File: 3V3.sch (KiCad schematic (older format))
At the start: 42 parts, among them U10 LM21215, U11 LM21215, U14 INA214, U15 INA214

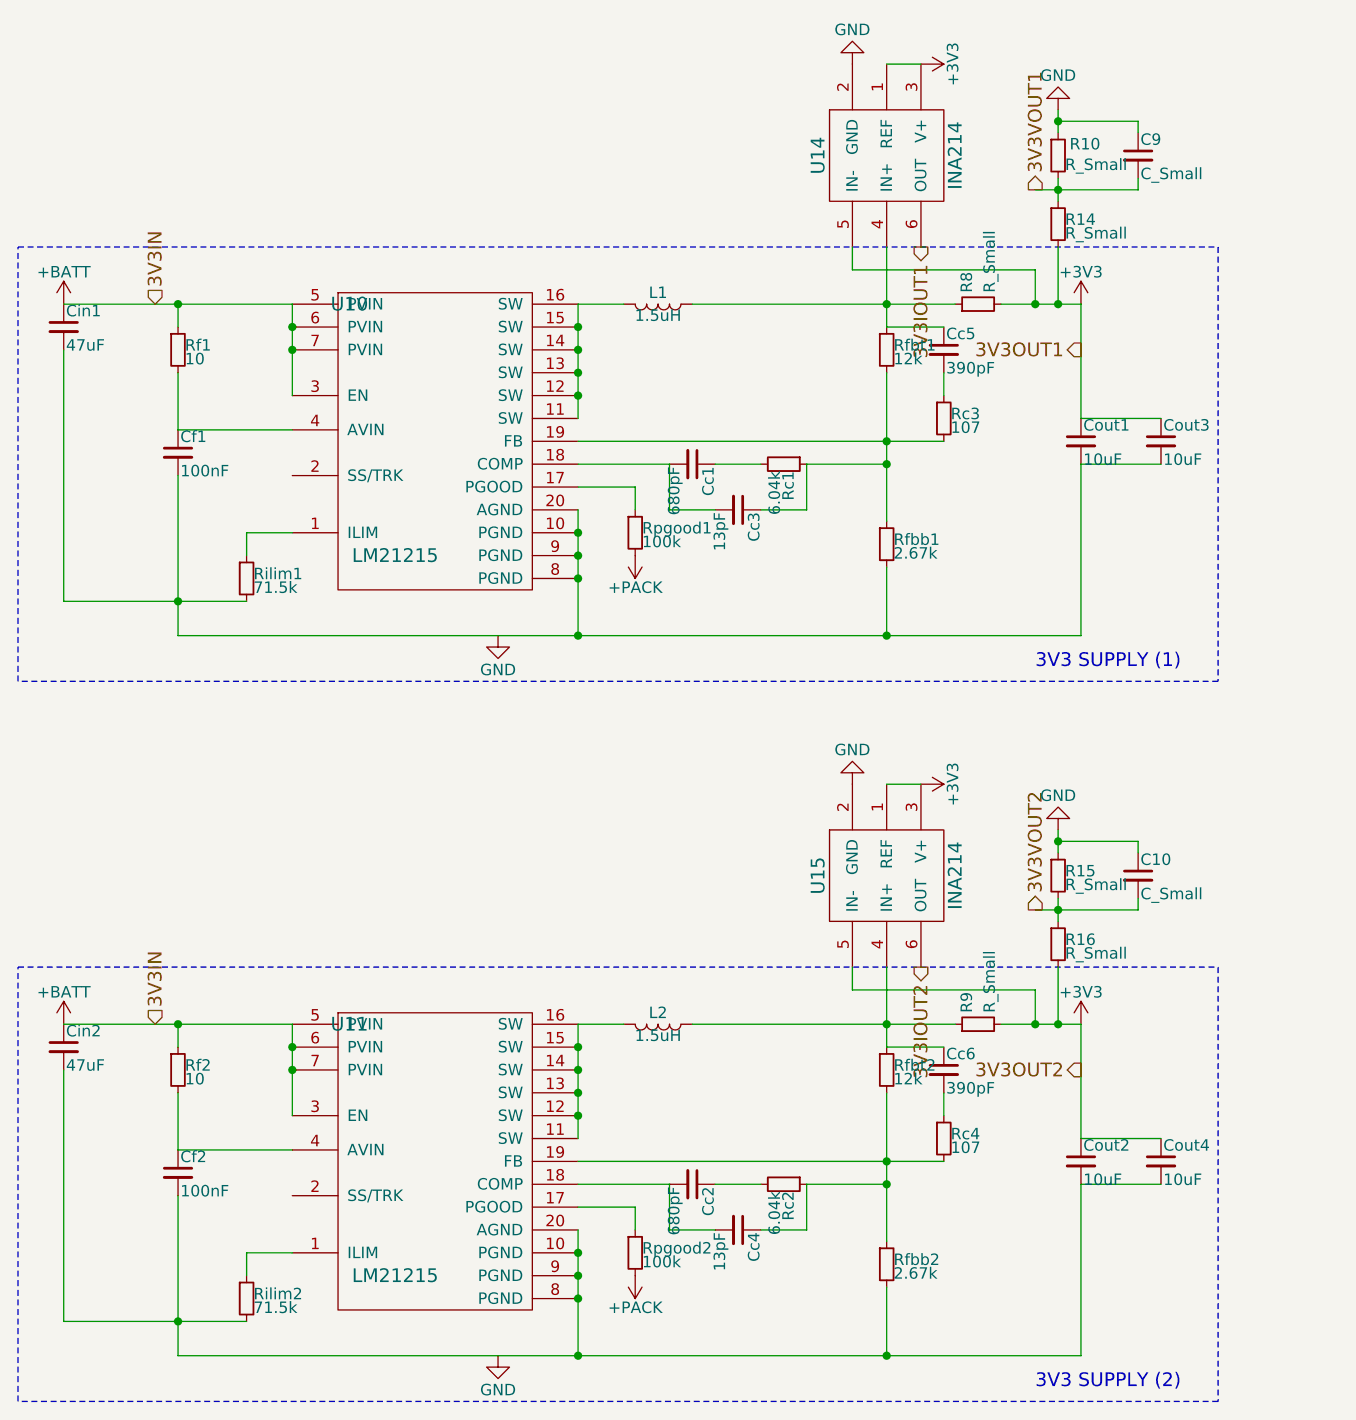
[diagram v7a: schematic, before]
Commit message: PCB layout as of 2018-02-12
All that’s left to do is add deployment switches
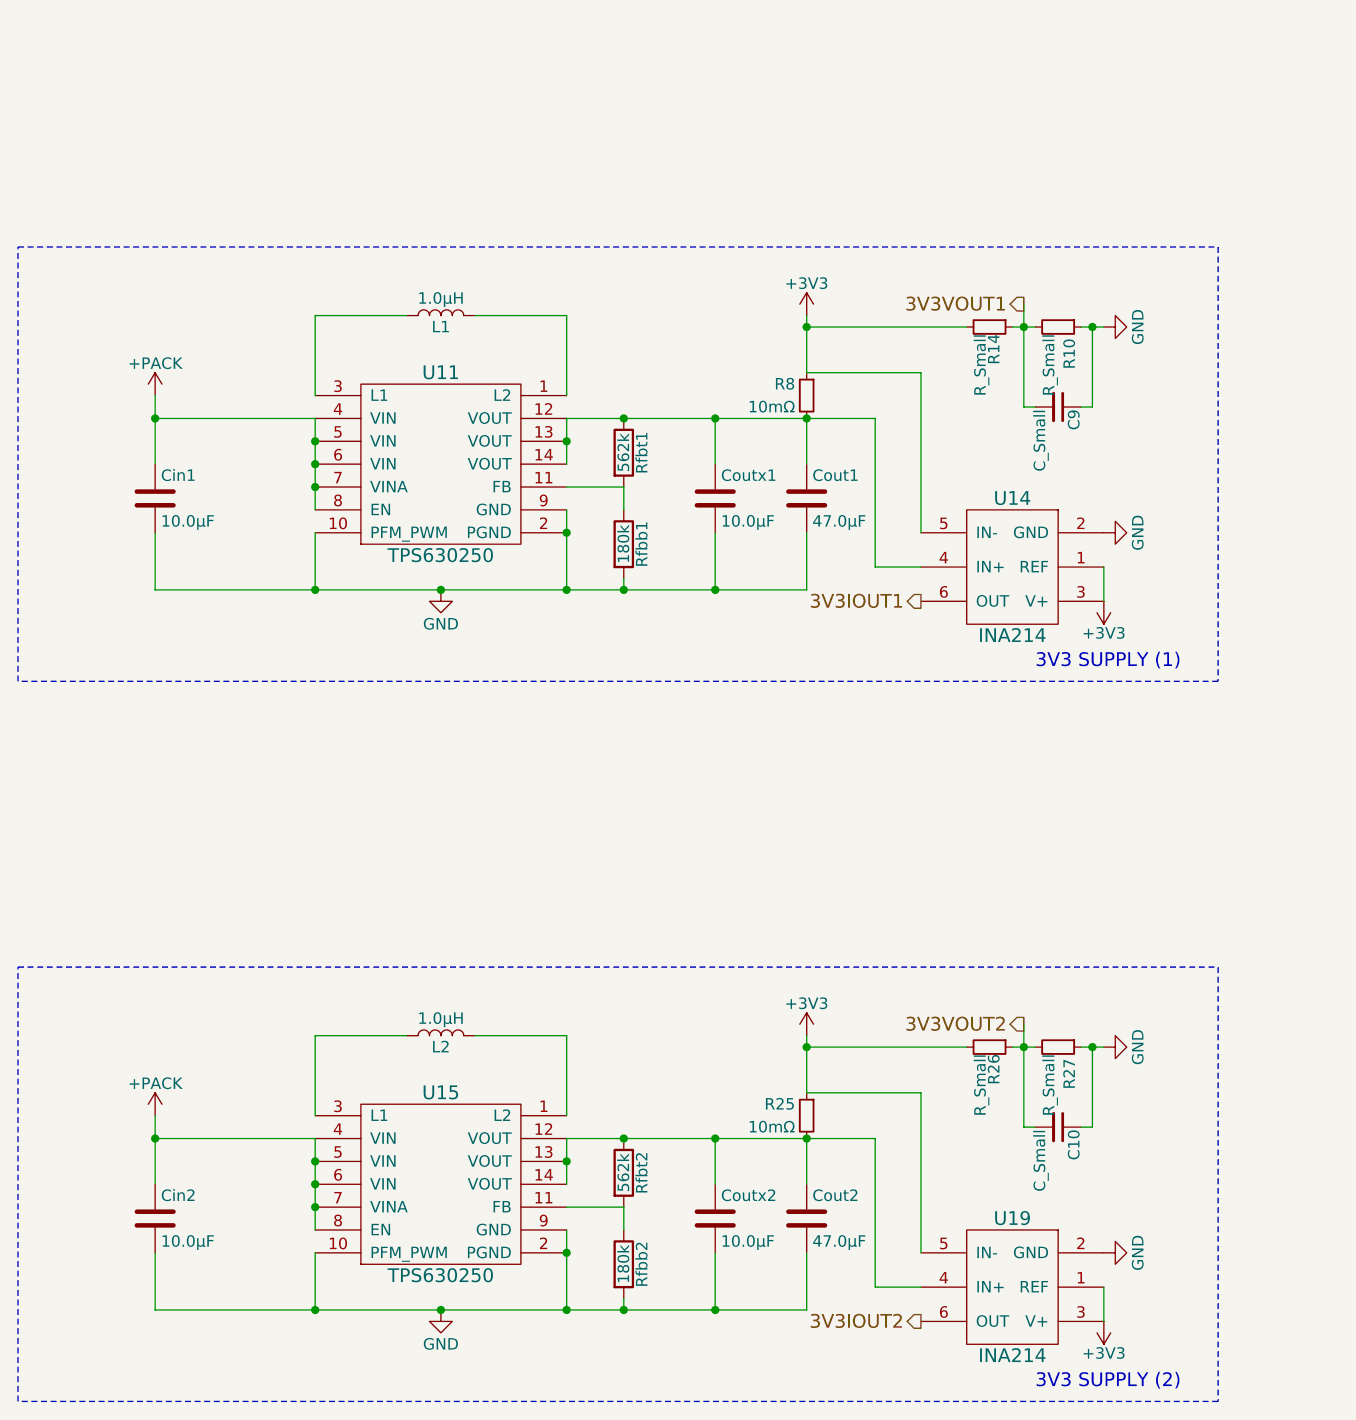
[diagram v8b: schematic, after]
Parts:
- removed Cc1, Cc2: 680pF, symbol C_Small
- removed Cc3, Cc4: 13pF, symbol C_Small
- removed Cc5, Cc6: 390pF, symbol C_Small
- removed Cf1, Cf2: 100nF, symbol C_Small
- removed Cin1, Cin2: 47uF, symbol C_Small
- removed Cout1, Cout2, Cout3, Cout4: 10uF, symbol C_Small
- removed R15, R16, R9: R_Small, symbol R_Small
- removed Rc1, Rc2: 6.04k, symbol R_Small
- removed Rc3, Rc4: 107, symbol R_Small
- removed Rf1, Rf2: 10, symbol R_Small
- removed Rfbb1, Rfbb2: 2.67k, symbol R_Small
- removed Rfbt1, Rfbt2: 12k, symbol R_Small
- removed Rilim1, Rilim2: 71.5k, symbol R_Small
- removed Rpgood1, Rpgood2: 100k, symbol R_Small
- removed U10, U11: LM21215, Housings_SSOP:HTSSOP-20-1EP_4.4x6.5mm_Pitch0.65mm_ThermalPad, symbol LM21215
- removed U15: INA214, symbol INA214
- added Cin1, Cin2, Coutx1, Coutx2: 10.0µF, Capacitors_SMD:C_0603_HandSoldering, symbol C
- added Cout1, Cout2: 47.0µF, Capacitors_SMD:C_0603_HandSoldering, symbol C
- added R25: 10mΩ, Resistors_SMD:R_0603_HandSoldering, symbol R_Small
- added R26, R27: R_Small, Resistors_SMD:R_0603_HandSoldering, symbol R_Small
- added Rfbb1, Rfbb2: 180k, Resistors_SMD:R_0603_HandSoldering, symbol R
- added Rfbt1, Rfbt2: 562k, Resistors_SMD:R_0603_HandSoldering, symbol R
- added U11, U15: TPS630250, eps-libraries:VQFN-14, symbol TPS630250
- added U19: INA214, kicad-libraries:SC70-6, symbol INA214
- C10, C9: footprint (none) -> Capacitors_SMD:C_0603_HandSoldering
- L1, L2: value 1.5uH -> 1.0µH; footprint (none) -> Inductors_SMD:L_Vishay_IHLP-1212
- R10, R14: footprint (none) -> Resistors_SMD:R_0603_HandSoldering
- R8: value R_Small -> 10mΩ; footprint (none) -> Resistors_SMD:R_0603_HandSoldering
- U14: footprint (none) -> kicad-libraries:SC70-6
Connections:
- net +3V3: now also R8.1, R25.1, R26.2, U19.1 (REF), U19.3 (V+), U19.5 (IN-); no longer R8.2
- net +PACK: now also Cin1.1, Cin2.1, U11.4 (VIN), U11.5 (VIN), U11.6 (VIN), U11.7 (VINA), U11.8 (EN), U15.4 (VIN), U15.5 (VIN), U15.6 (VIN), U15.7 (VINA), U15.8 (EN)
- net 3V3IOUT2: now also U19.6 (OUT)
- net 3V3VOUT2: now also R26.1, R27.2
- net GND: now also Cin1.2, Cin2.2, Cout1.2, Cout2.2, Coutx1.2, Coutx2.2, R27.1, Rfbb1.2, Rfbb2.2, U11.10 (PFM_PWM), U11.2 (PGND), U11.9 (GND), U15.10 (PFM_PWM), U15.2 (PGND), U15.9 (GND), U19.2 (GND)
- net at L1.2: now also U11.1 (L2)
- net at L2.2: now also U15.1 (L2)
- net at L2.1: now also U15.3 (L1)
- new net: Cout1.1, Coutx1.1, R8.2, Rfbt1.1, U11.12 (VOUT), U11.13 (VOUT), U11.14 (VOUT), U14.4 (IN+)
- new net: Rfbb1.1, Rfbt1.2, U11.11 (FB)
- new net: L1.1, U11.3 (L1)
- new net: Cout2.1, Coutx2.1, R25.2, Rfbt2.1, U15.12 (VOUT), U15.13 (VOUT), U15.14 (VOUT), U19.4 (IN+)
- new net: Rfbb2.1, Rfbt2.2, U15.11 (FB)
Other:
- moved on the sheet: C9, R10, R14, R8, U14
